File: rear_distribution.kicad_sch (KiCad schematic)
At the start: 57 parts, among them J11 Conn_01x35, J21 Conn_01x23, J31 Conn_01x23, J41 Conn_01x23, J51 Conn_01x08, J61 Conn_01x08, J71 Conn_01x02, J72 Conn_01x02, J73 Conn_01x04, J74 Conn_01x02, J81 Conn_01x02, J82 Conn_01x02, J83 Conn_01x04, J84 Conn_01x03, J85 Conn_01x08, K1 G2RL-1A, Q1 DMN6075S, Q2 DMN6075S

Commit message: schematic: Rename some nets to match naming scheme
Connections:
- net BMS_INDICATOR_GND renamed GND_BMS_INDICATOR
- net IMD_INDICATOR_GND renamed GND_IMD_INDICATOR
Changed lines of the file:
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@@
 		)
 	)
-	(global_label "IMD_INDICATOR_GND"
+	(global_label "GND_IMD_INDICATOR"
 		(shape output)
 		(at 26.67 257.81 0)
@@
 		)
 	)
-	(global_label "IMD_INDICATOR_GND"
+	(global_label "GND_IMD_INDICATOR"
 		(shape input)
 		(at 96.52 111.76 0)
@@
 		)
 	)
-	(global_label "BMS_INDICATOR_GND"
+	(global_label "GND_BMS_INDICATOR"
 		(shape output)
 		(at 26.67 255.27 0)
@@
 		)
 	)
-	(global_label "BMS_INDICATOR_GND"
+	(global_label "GND_BMS_INDICATOR"
 		(shape input)
 		(at 96.52 127 0)

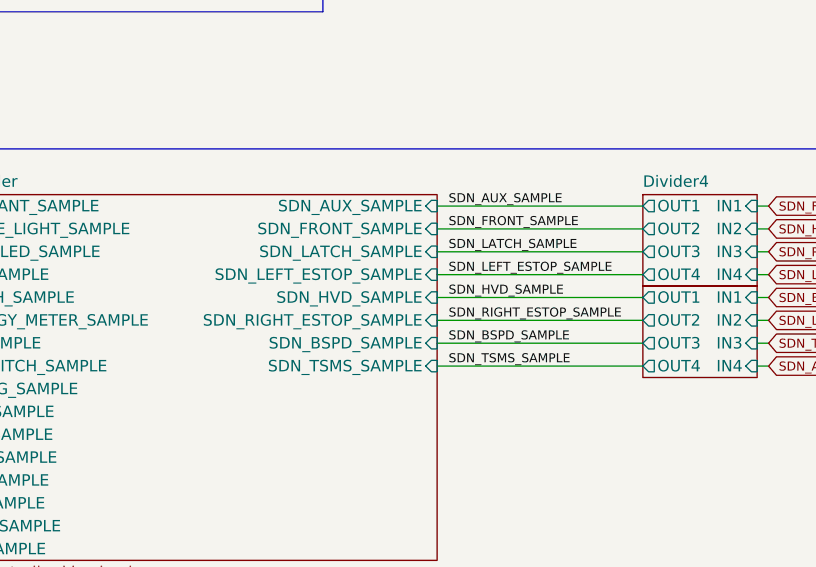
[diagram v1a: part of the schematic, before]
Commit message: *: Fix shutdown labelling mismatch
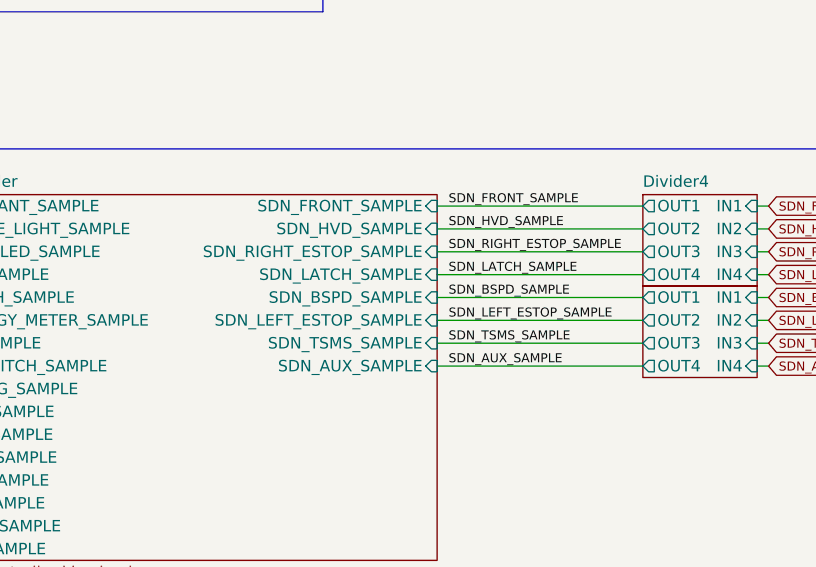
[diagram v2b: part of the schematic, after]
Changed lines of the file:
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@@
 	)
 	(label "SDN_TSMS_SAMPLE"
-		(at 261.62 207.01 0)
+		(at 261.62 204.47 0)
 		(effects
 			(font
@@
 	)
 	(label "SDN_AUX_SAMPLE"
-		(at 261.62 189.23 0)
+		(at 261.62 207.01 0)
 		(effects
 			(font
@@
 	)
 	(label "SDN_BSPD_SAMPLE"
-		(at 261.62 204.47 0)
+		(at 261.62 199.39 0)
 		(effects
 			(font
@@
 	)
 	(label "SDN_RIGHT_ESTOP_SAMPLE"
-		(at 261.62 201.93 0)
+		(at 261.62 194.31 0)
 		(effects
 			(font
@@
 	)
 	(label "SDN_HVD_SAMPLE"
-		(at 261.62 199.39 0)
+		(at 261.62 191.77 0)
 		(effects
 			(font
@@
 	)
 	(label "SDN_LEFT_ESTOP_SAMPLE"
-		(at 261.62 196.85 0)
+		(at 261.62 201.93 0)
 		(effects
 			(font
@@
 	)
 	(label "SDN_FRONT_SAMPLE"
-		(at 261.62 191.77 0)
+		(at 261.62 189.23 0)
 		(effects
 			(font
@@
 	)
 	(label "SDN_LATCH_SAMPLE"
-		(at 261.62 194.31 0)
+		(at 261.62 196.85 0)
 		(effects
 			(font
@@
 		)
 		(pin "SDN_BSPD_SAMPLE" input
-			(at 260.35 204.47 0)
+			(at 260.35 199.39 0)
 			(effects
 				(font
@@
 		)
 		(pin "SDN_LATCH_SAMPLE" input
-			(at 260.35 194.31 0)
+			(at 260.35 196.85 0)
 			(effects
 				(font
@@
 		)
 		(pin "SDN_LEFT_ESTOP_SAMPLE" input
-			(at 260.35 196.85 0)
+			(at 260.35 201.93 0)
 			(effects
 				(font
@@
 		)
 		(pin "SDN_RIGHT_ESTOP_SAMPLE" input
-			(at 260.35 201.93 0)
+			(at 260.35 194.31 0)
 			(effects
 				(font
@@
 		)
 		(pin "SDN_AUX_SAMPLE" input
-			(at 260.35 189.23 0)
+			(at 260.35 207.01 0)
 			(effects
 				(font
@@
 		)
 		(pin "SDN_HVD_SAMPLE" input
-			(at 260.35 199.39 0)
+			(at 260.35 191.77 0)
 			(effects
 				(font
@@
 		)
 		(pin "SDN_TSMS_SAMPLE" input
-			(at 260.35 207.01 0)
+			(at 260.35 204.47 0)
 			(effects
 				(font
@@
 		)
 		(pin "SDN_FRONT_SAMPLE" input
-			(at 260.35 191.77 0)
+			(at 260.35 189.23 0)
 			(effects
 				(font
